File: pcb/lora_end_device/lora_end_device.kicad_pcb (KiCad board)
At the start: 2 copper layers, 60 x 41 mm, 31 parts, among them J1 USB_B_Micro, J2 UFL, J3 SMA, J4 UART, J5 Reset, J6 PRG, J7 Sensor, U2 MCP6021, U3 LD1117, U4 RFM95W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

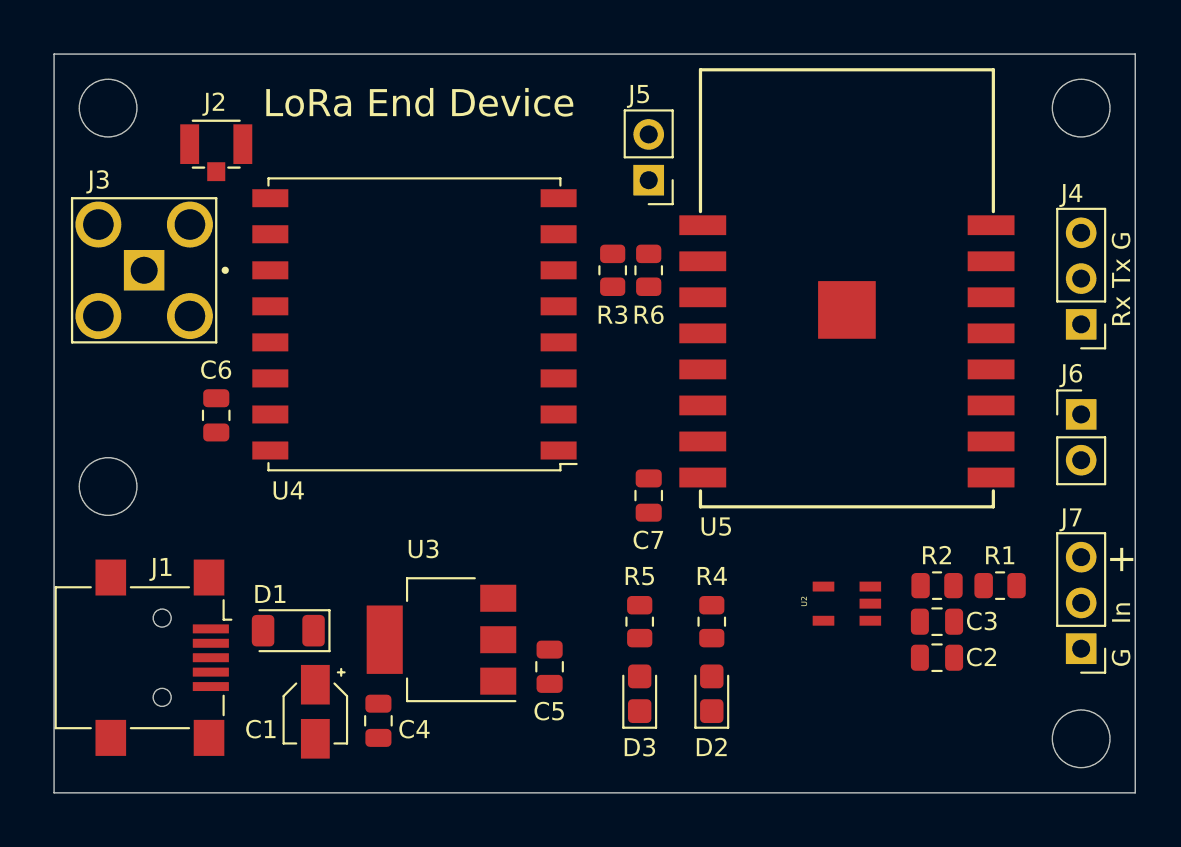
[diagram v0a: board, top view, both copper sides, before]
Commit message: reubicación de conector SMA
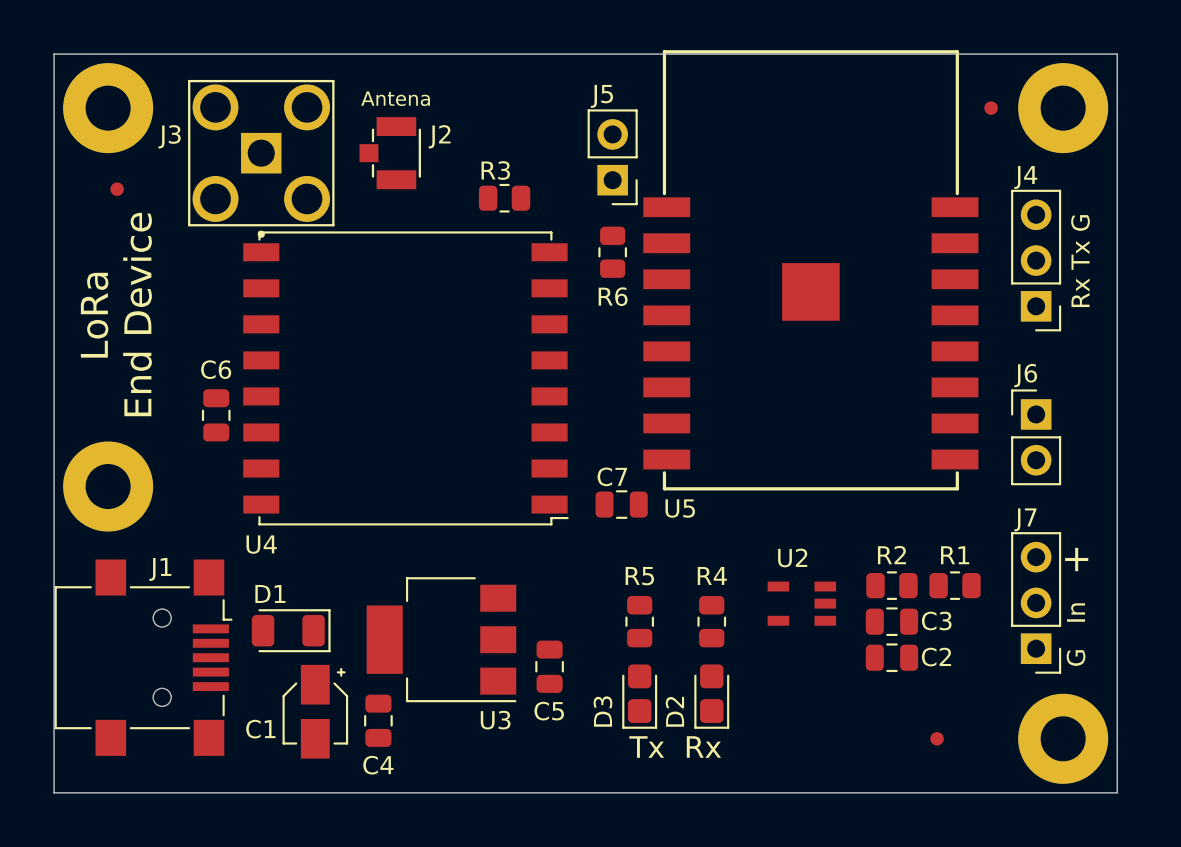
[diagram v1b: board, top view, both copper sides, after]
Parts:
- added FID1: Fiducial, Fiducial:Fiducial_0.75mm_Mask1.5mm, F.Cu at (61.5, 65.5)
- added FID2: Fiducial, Fiducial:Fiducial_0.75mm_Mask1.5mm, F.Cu at (110.0, 61.0)
- added FID3: Fiducial, Fiducial:Fiducial_0.75mm_Mask1.5mm, F.Cu at (107.0, 96.0)
- D2: value Led Rx -> Verde
- D3: value Led Tx -> Rojo
- H1, H2, H3, H4: footprint MountingHole:MountingHole_3.2mm_M3 -> MountingHole:MountingHole_2.5mm_Pad
- moved J2 10.0 mm to (77.0, 63.5), turned to 270 degrees
- moved J3 9.19 mm to (69.5, 63.5), turned to 180 degrees
- moved R3 7.21 mm to (83.0, 66.0), turned to 0 degrees
- moved U4 3.04 mm to (77.5, 76.0)
- moved J4 2.69 mm to (112.5, 72.0)
- moved C2 2.50 mm to (104.5, 91.5)
- moved C3 2.50 mm to (104.5, 89.5)
- moved J6 2.50 mm to (112.5, 78.0)
- moved J7 2.50 mm to (112.5, 91.0)
- moved R1 2.50 mm to (108.0, 87.5)
- moved R2 2.50 mm to (104.5, 87.5)
- moved U2 2.50 mm to (99.5, 88.5)
- moved R6 2.24 mm to (89.0, 69.0)
- moved U5 2.24 mm to (100.0, 70.0)
- moved J5 2.00 mm to (89.0, 65.0)
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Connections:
- H1 pad 1: (no net) -> GND
- H2 pad 1: (no net) -> GND
- H3 pad 1: (no net) -> GND
- H4 pad 1: (no net) -> GND
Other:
- board size 60 x 41 mm -> 59 x 41 mm
- board text added: "Antena"
- board text added: "LoRa End Device V1.0"
- board text added: "Tx Rx"

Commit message: add ruteo
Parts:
- moved C2 4.50 mm to (104.5, 87.0)
- moved C3 1.50 mm to (104.5, 91.0)
- moved C5 1.50 mm to (85.5, 93.5)
- moved R2 1.50 mm to (104.5, 89.0)
- moved C4 1.41 mm to (77.0, 96.0), turned to 0 degrees
- moved R1 0.50 mm to (108.0, 87.0)
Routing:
- net +3V3: track 0.00 -> 128.6 mm, vias 0 -> 2
- net Net-(U4-Pad14): track 0.00 -> 42.8 mm, vias 0 -> 2
- net Net-(U4-Pad15): track 0.00 -> 42.4 mm, vias 0 -> 2
- net Net-(R3-Pad1): track 0.00 -> 39.2 mm, vias 0 -> 2
- net /Analog0: track 0.00 -> 32.5 mm
- net Net-(J6-Pad1): track 0.00 -> 30.5 mm, vias 0 -> 2
- net Net-(R4-Pad1): track 0.00 -> 21.5 mm, vias 0 -> 2
- net Net-(C1-Pad1): track 0.00 -> 19.2 mm
- net Net-(U4-Pad3): track 0.00 -> 12.5 mm
- net Net-(J2-Pad2): track 0.00 -> 11.5 mm
- net GND: track 0.00 -> 11.3 mm
- net Net-(U4-Pad2): track 0.00 -> 8.36 mm
- net Net-(U4-Pad4): track 0.00 -> 7.54 mm
- net Net-(J5-Pad1): track 0.00 -> 6.71 mm
- net Net-(U4-Pad6): track 0.00 -> 6.71 mm
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- added copper zone on B.Cu, net GND
- added copper zone on F.Cu, net GND
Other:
- outline, holes or cut-outs redrawn
- board text added: "1.0.0"
- board text added: "5 Vcc"
- board text added: "915 MHz"
- board text added: "Alimentación"
- board text added: "Frecuencia"
- board text added: "LoRaWAN End Device"
- board text added: "Material: FR4 Espesor: 1.6mm Terminación superficial: HASL Color máscara: negro Color serigrafía superior: blanco Color serigrafía inferior: blanco"
- board text added: "PRG"
- board text added: "Reset"
- board text added: "Sensor"
- board text added: "UART"
- board text added: "Versión Hardware"
- board text added: "Versión firmware"
- board text removed: "LoRa End Device"
- board text removed: "LoRa End Device V1.0"

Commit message: correcciones revisiones del docente
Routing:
- net +3V3: track 128.6 -> 133.9 mm
- net GND: track 11.3 -> 15.3 mm
- net Net-(U4-Pad3): track 12.5 -> 14.2 mm
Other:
- net class Default: clearance 0.2 -> 0.4; trace_width 0.25 -> 0.3
- rule trace_clearance: 0.2 -> 0.4
- board text added: "Industria Argentina"
- board text added: "Mínimos (Mayer 10 mils): Grillas: 1mm, 0,5 mm Vía: 0,8/0,4 Márgen: 1mm Pista: 0,25mm/0,3MM"
- board text added: "mcastello Ingeniería 2021"
- board text removed: "mcastello Ingeniería"

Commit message: Correcciones finales
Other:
- net class Default: clearance 0.4 -> 0.3; trace_width 0.3 -> 0.4
- rule trace_clearance: 0.4 -> 0.3
- board text added: "Diseñado en Argentina"
- board text added: "Mínimos (Mayer 10 mils): Grillas: 1mm, 0,5 mm Vía: 0,8/0,4 Pista: 0,25mm/0,3MM Clearance: 0,3 mm"
- board text removed: "Industria Argentina"
- board text removed: "Mínimos (Mayer 10 mils): Grillas: 1mm, 0,5 mm Vía: 0,8/0,4 Márgen: 1mm Pista: 0,25mm/0,3MM"
